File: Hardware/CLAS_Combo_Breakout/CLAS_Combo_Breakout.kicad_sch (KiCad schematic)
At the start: 77 parts, among them J1 USB_C_Receptacle_USB2.0, J2 USB_C_Receptacle_USB2.0, J3 Conn_SMA, U1 USBLC6-2P6, U2 ZED-F9P, U3 NEO-D9C-00B, U4 USBLC6-2P6, U5 LMV331, U6 AP2112K-3.3, U7 DSS20200, U8 BP2G1+, U9 NT1191GEAE3S

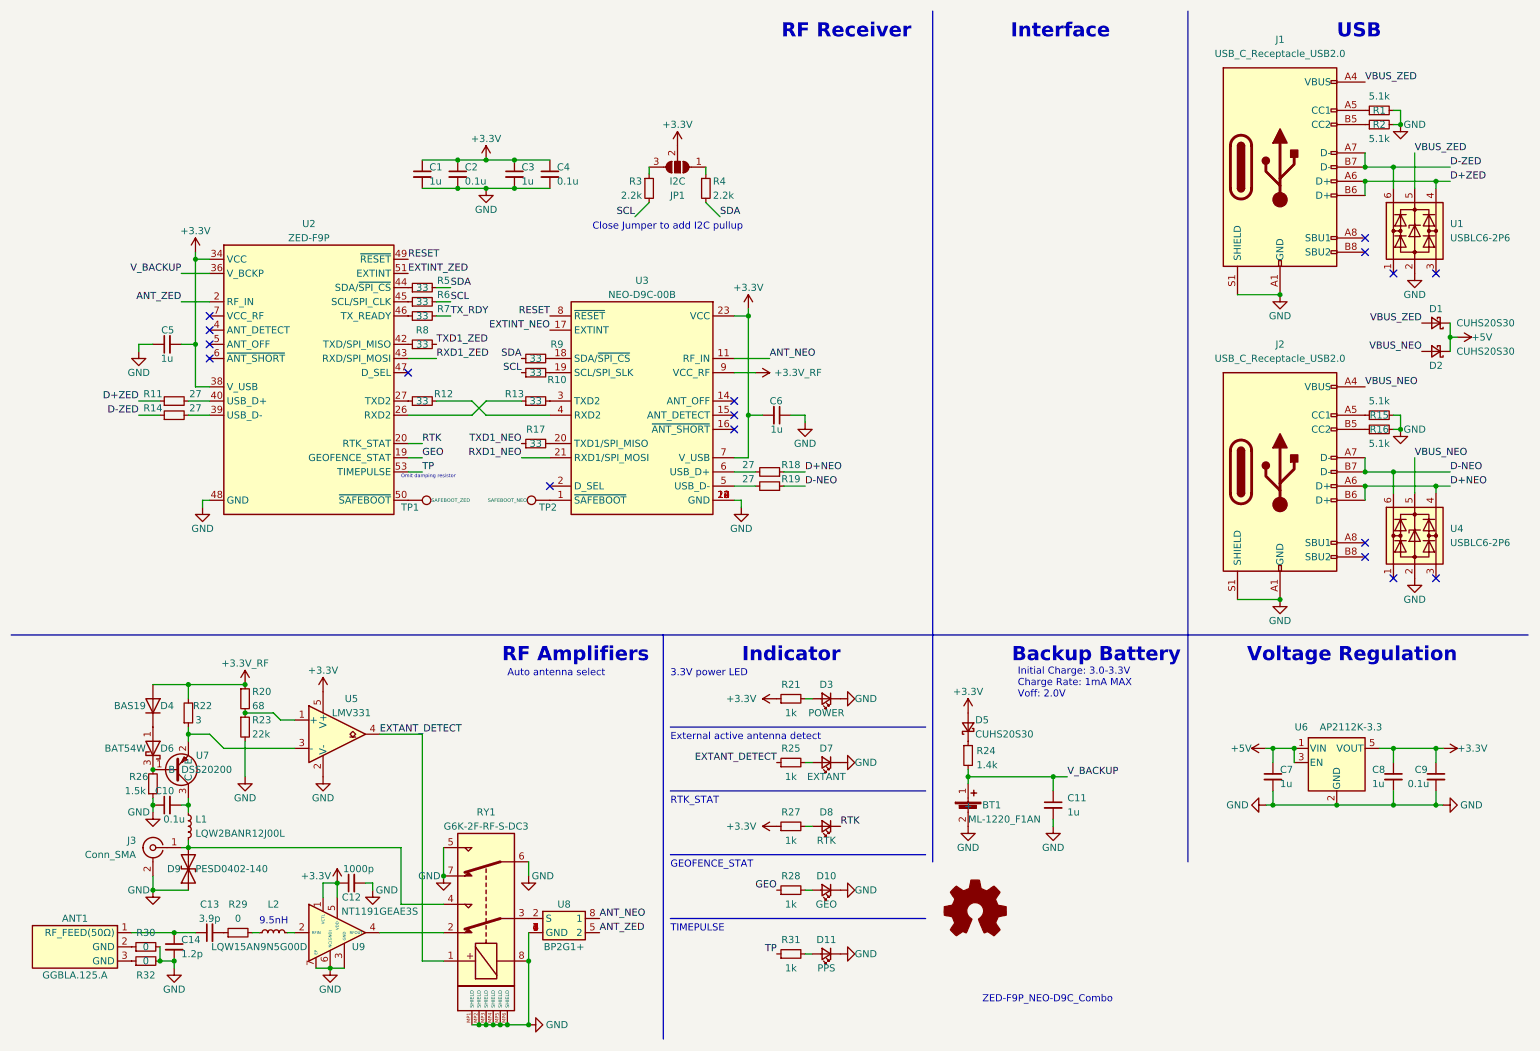
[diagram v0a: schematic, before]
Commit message: 部品を配置
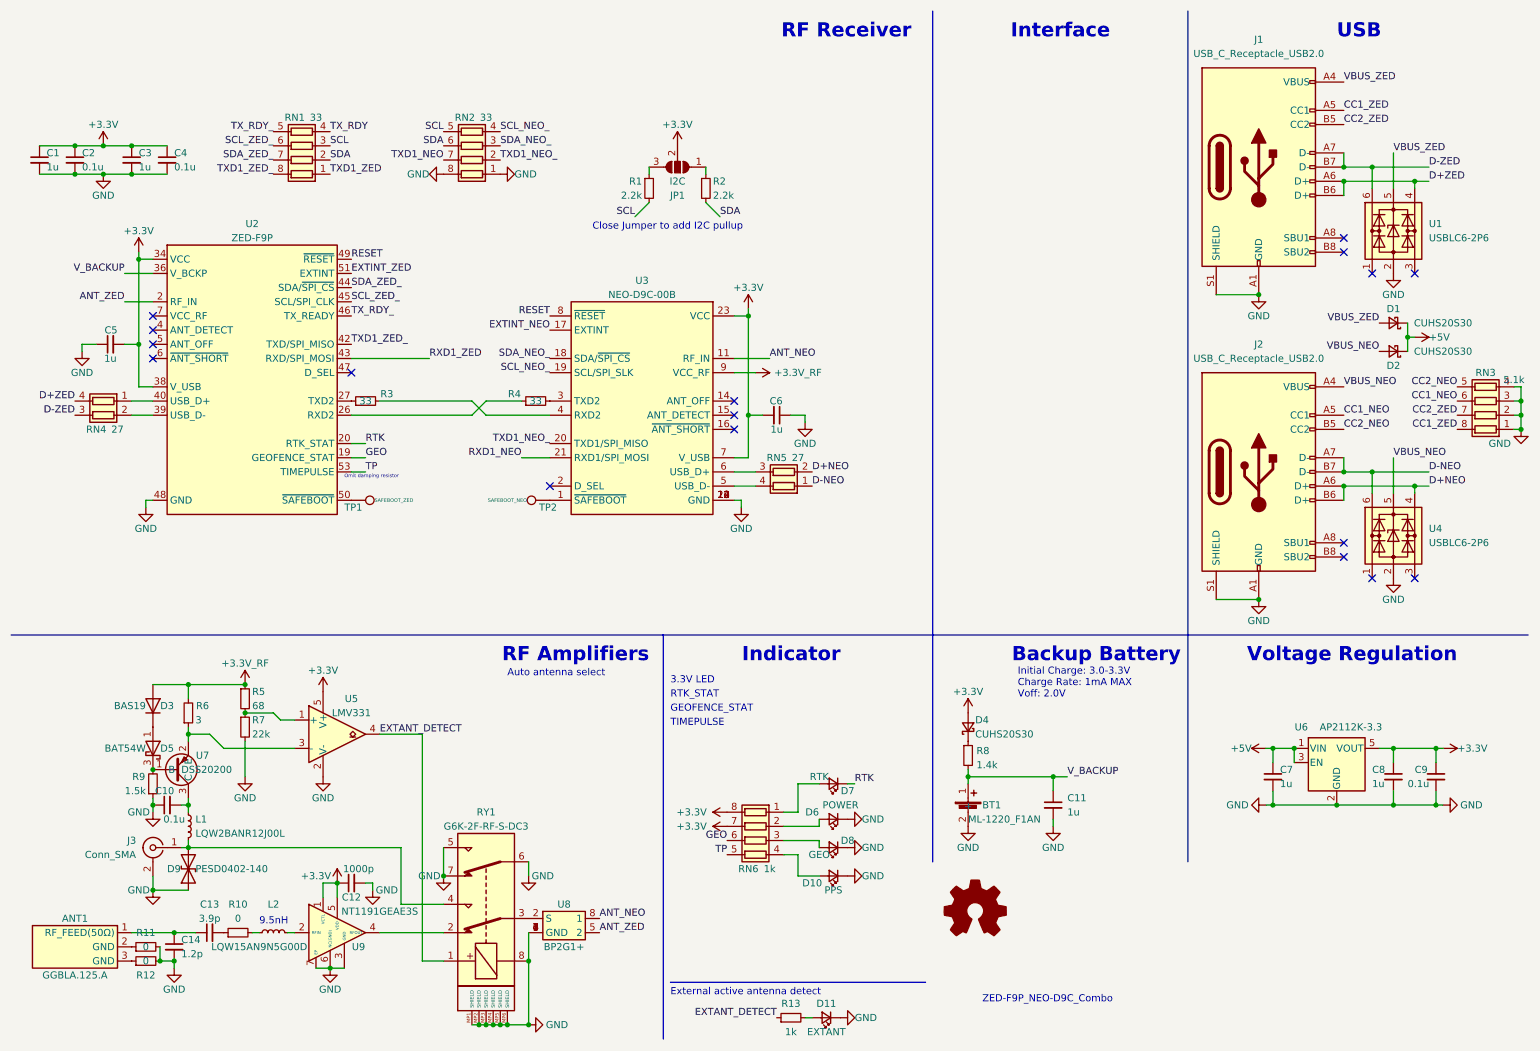
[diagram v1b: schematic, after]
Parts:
- removed R1, R15, R16, R2: 5.1k, Resistor_SMD:R_0603_1608Metric, symbol Device:R_Small
- removed R10, R17, R5, R6, R7, R8, R9: 33, Resistor_SMD:R_0603_1608Metric, symbol Device:R_Small
- removed R11, R14, R18, R19: 27, Resistor_SMD:R_0603_1608Metric, symbol Device:R_Small
- removed R21, R27, R28, R31: 1k, Resistor_SMD:R_0603_1608Metric, symbol Device:R_Small
- added RN1, RN2: 33, Resistor_SMD:R_Array_Convex_4x0402, symbol Device:R_Pack04
- added RN3: 5.1k, Resistor_SMD:R_Array_Convex_4x0402, symbol Device:R_Pack04
- added RN4, RN5: 27, Resistor_SMD:R_Array_Convex_2x0402, symbol Device:R_Pack02
- added RN6: 1k, Resistor_SMD:R_Array_Convex_4x0402, symbol Device:R_Pack04
- J1, J2: footprint Connector_USB:USB_C_Receptacle_GCT_USB4085 -> Connector_USB_extlib:USB_C_Receptacle_GCT_USB4120-03-C
- renumbered D11 to D10, D7 to D11, D4 to D3, D5 to D4, D6 to D5, D3 to D6, D8 to D7, D10 to D8, R3 to R1, R29 to R10, R30 to R11, R32 to R12, R25 to R13, R4 to R2, R12 to R3, R13 to R4, R20 to R5, R22 to R6, R23 to R7, R24 to R8, R26 to R9
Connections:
- net +3.3V: now also RN6.7 (R2.2), RN6.8 (R1.2)
- net D+NEO: now also RN5.2 (R2.1)
- net D+ZED: now also RN4.4 (R1.2)
- net D-NEO: now also RN5.1 (R1.1)
- net D-ZED: now also RN4.3 (R2.2)
- net GEO: now also RN6.6 (R3.2)
- net GND: now also RN2.1 (R1.1), RN2.8 (R1.2), RN3.1 (R1.1), RN3.2 (R2.1), RN3.3 (R3.1), RN3.4 (R4.1)
- net SCL: now also RN1.3 (R3.1), RN2.5 (R4.2)
- net SDA: now also RN1.2 (R2.1), RN2.6 (R3.2)
- net TP: now also RN6.5 (R4.2)
- net TXD1_NEO: now also RN2.7 (R2.2)
- net TXD1_ZED: now also RN1.1 (R1.1)
- net TX_RDY: now also RN1.4 (R4.1)
- net at D6.2 (A): now also RN6.2 (R2.1)
- net SCL_NEO_: now reaches U3.19 (SCL/SPI_SLK)
- net SCL_NEO_: now also RN2.4 (R4.1)
- net at D7.2 (A): now also RN6.1 (R1.1)
- net SCL_ZED_: now reaches U2.45 (SCL/SPI_CLK)
- net SCL_ZED_: now also RN1.6 (R3.2)
- net at D10.2 (A): now also RN6.4 (R4.1)
- net at U2.40 (USB_D+): now also RN4.1 (R1.1)
- net SDA_ZED_: now reaches U2.44 (SDA/~{SPI_CS})
- net SDA_ZED_: now also RN1.7 (R2.2)
- net CC1_NEO: now reaches J2.A5 (CC1)
- net CC1_NEO: now also RN3.6 (R3.2)
- net CC2_NEO: now reaches J2.B5 (CC2)
- net CC2_NEO: now also RN3.5 (R4.2)
- net TX_RDY_: now reaches U2.46 (TX_READY)
- net TX_RDY_: now also RN1.5 (R4.2)
- net CC2_ZED: now reaches J1.B5 (CC2)
- net CC2_ZED: now also RN3.7 (R2.2)
- net at D8.2 (A): now also RN6.3 (R3.1)
- net CC1_ZED: now reaches J1.A5 (CC1)
- net CC1_ZED: now also RN3.8 (R1.2)
- net at U3.6 (USB_D+): now also RN5.3 (R2.2)
- net at U2.39 (USB_D-): now also RN4.2 (R2.1)
- net TXD1_ZED_: now reaches U2.42 (TXD/SPI_MISO)
- net TXD1_ZED_: now also RN1.8 (R1.2)
- net TXD1_NEO_: now reaches U3.20 (TXD1/SPI_MISO)
- net TXD1_NEO_: now also RN2.2 (R2.1)
- net SDA_NEO_: now reaches U3.18 (SDA/~{SPI_CS})
- net SDA_NEO_: now also RN2.3 (R3.1)
- net at U3.5 (USB_D-): now also RN5.4 (R1.2)
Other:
- note added: "3.3V LED"
- note removed: "3.3V power LED"
- moved on the sheet: C1, C2, C3, C4, C5, D1, D10, D11, D2, D6, D7, D8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

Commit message: RFリレーとスプリッタを置き換え
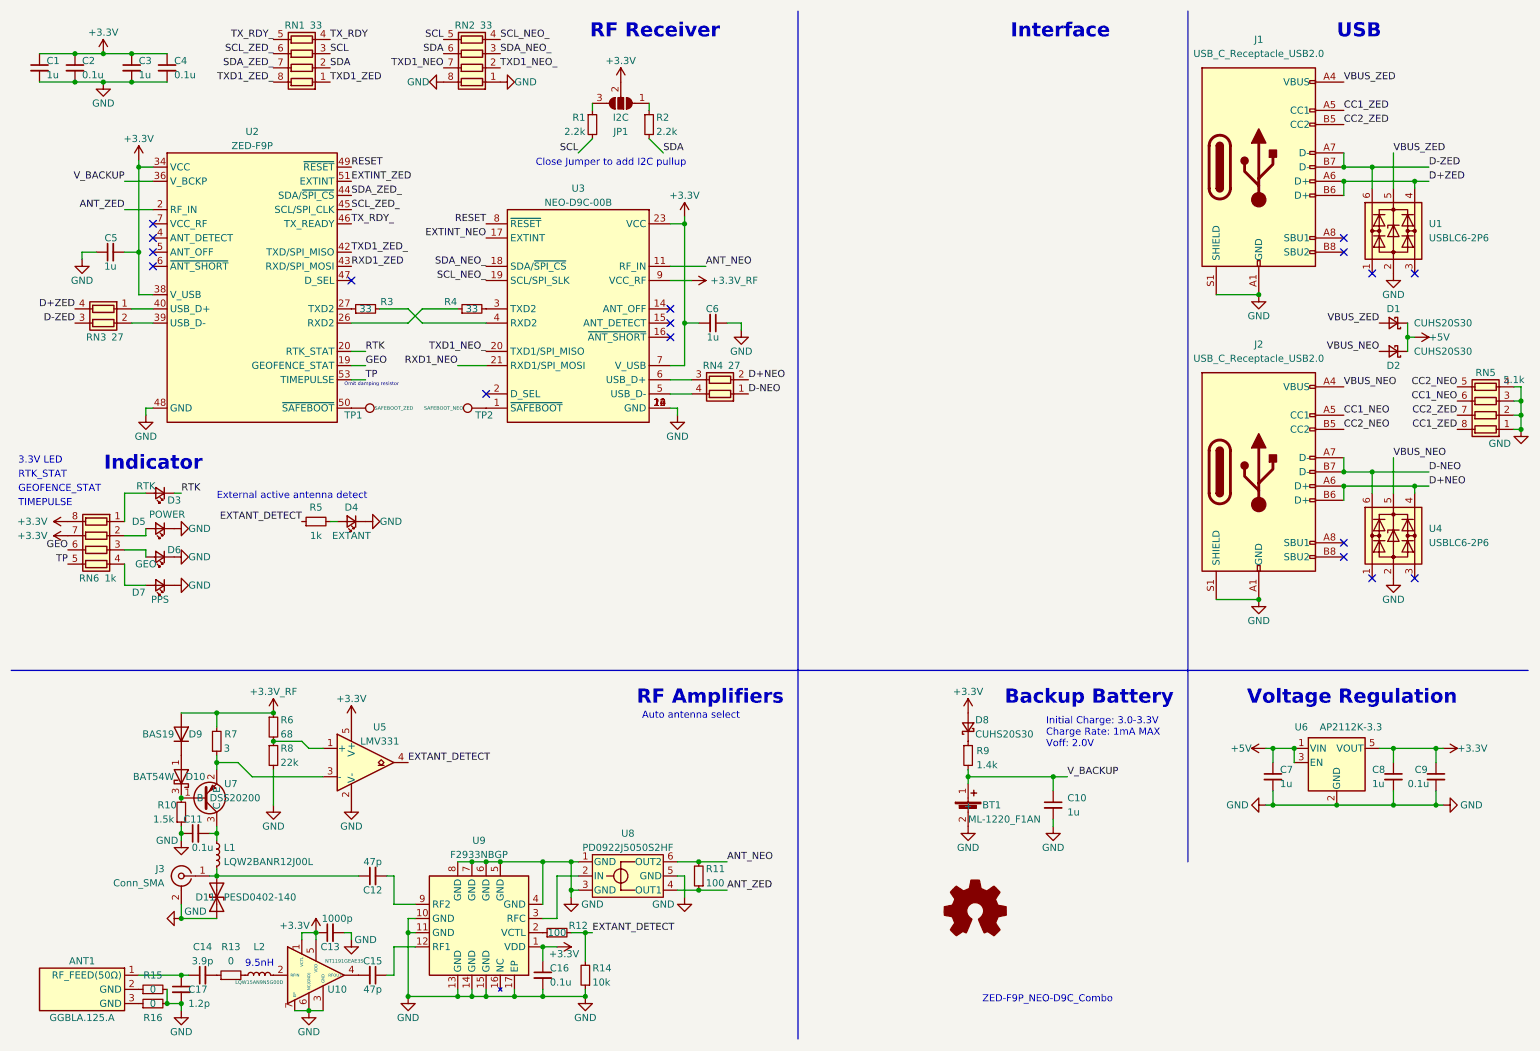
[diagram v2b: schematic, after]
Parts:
- removed RY1: G6K-2F-RF-S-DC3, G6K-2F-RF-S-DC3:G6K-2F-RF-S-DC3, symbol G6K-2F-RF-S-DC3:G6K-2F-RF-S-DC3
- removed U8: BP2G1+, BP2G1+:BP2G1, symbol BP2G1+:BP2G1+
- added C12, C15: 47p, Capacitor_SMD:C_0603_1608Metric, symbol Device:C_Small
- added C16: 0.1u, Capacitor_SMD:C_0603_1608Metric, symbol Device:C_Small
- added R11, R12: 100, Resistor_SMD:R_0603_1608Metric, symbol Device:R_Small
- added R14: 10k, Resistor_SMD:R_0603_1608Metric, symbol Device:R_Small
- added U8: PD0922J5050S2HF, PD0922J5050S2HF:PD0922J5050S2HF_ANA, symbol PD0922J5050S2HF:PD0922J5050S2HF
- added U9: F2933NBGP, F2933NBGP:F2933NBGP, symbol F2933NBGP:F2933NBGP
- renumbered C11 to C10, C10 to C11, C12 to C13, C13 to C14, C14 to C17, D5 to D10, D9 to D11, D7 to D3, D11 to D4, D6 to D5, D8 to D6, D10 to D7, D4 to D8, D3 to D9, R9 to R10, R10 to R13, R11 to R15, R12 to R16, R13 to R5, R5 to R6, R6 to R7, R7 to R8, R8 to R9, RN4 to RN3, RN5 to RN4, RN3 to RN5, U9 to U10
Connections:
- net +3.3V: now also C16.1, U9.1 (VDD)
- net ANT_NEO: now also R11.2, U8.6 (OUT2)
- net ANT_ZED: now also R11.1, U8.4 (OUT1)
- net EXTANT_DETECT: now also R12.2, R14.2
- net GND: now also C16.2, R14.1, U8.1 (GND), U8.3 (GND), U8.5 (GND), U9.10 (GND), U9.11 (GND), U9.13 (GND), U9.14 (GND), U9.15 (GND), U9.17 (EP), U9.4 (GND), U9.5 (GND), U9.6 (GND), U9.7 (GND), U9.8 (GND)
- net at U10.4 (RFOUT): now also C15.2
- net at D11.2 (A2), J3.1 (In), L1.2: now also C12.1
- new net: U8.2 (IN), U9.3 (RFC)
- new net: C15.1, U9.12 (RF1)
- new net: R12.1, U9.2 (VCTL)
- new net: C12.2, U9.9 (RF2)
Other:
- moved on the sheet: ANT1, C1, C11, C13, C14, C17, C2, C3, C4, C5, C6, D10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

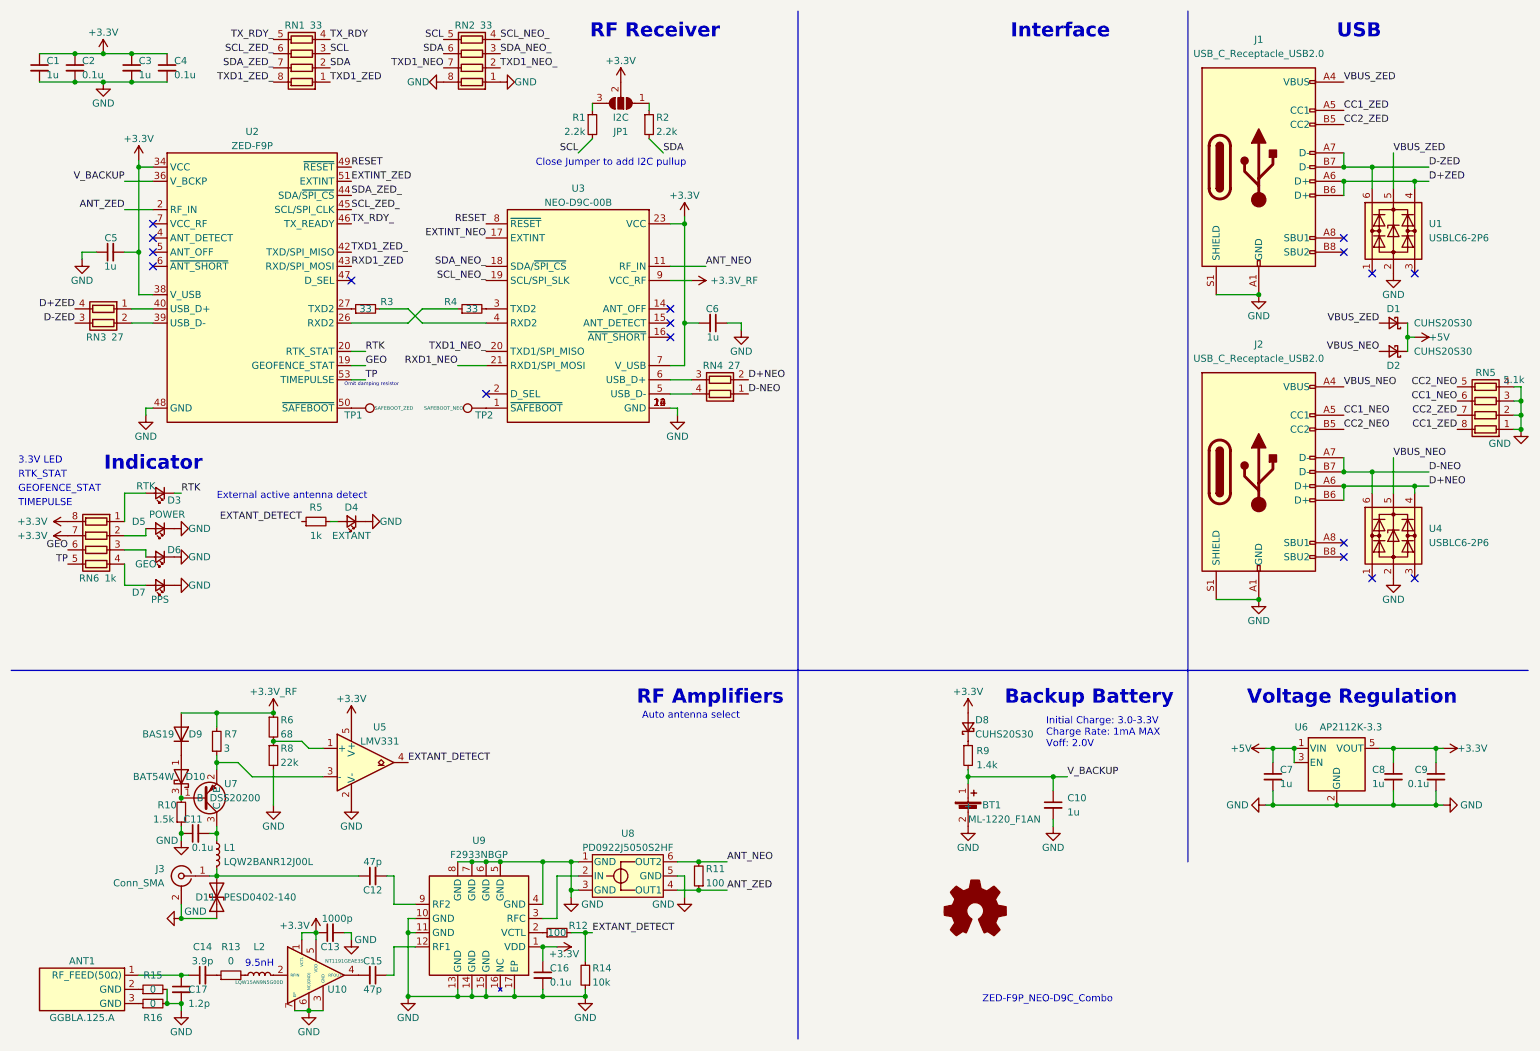
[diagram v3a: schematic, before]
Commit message: change BAT and USB_C
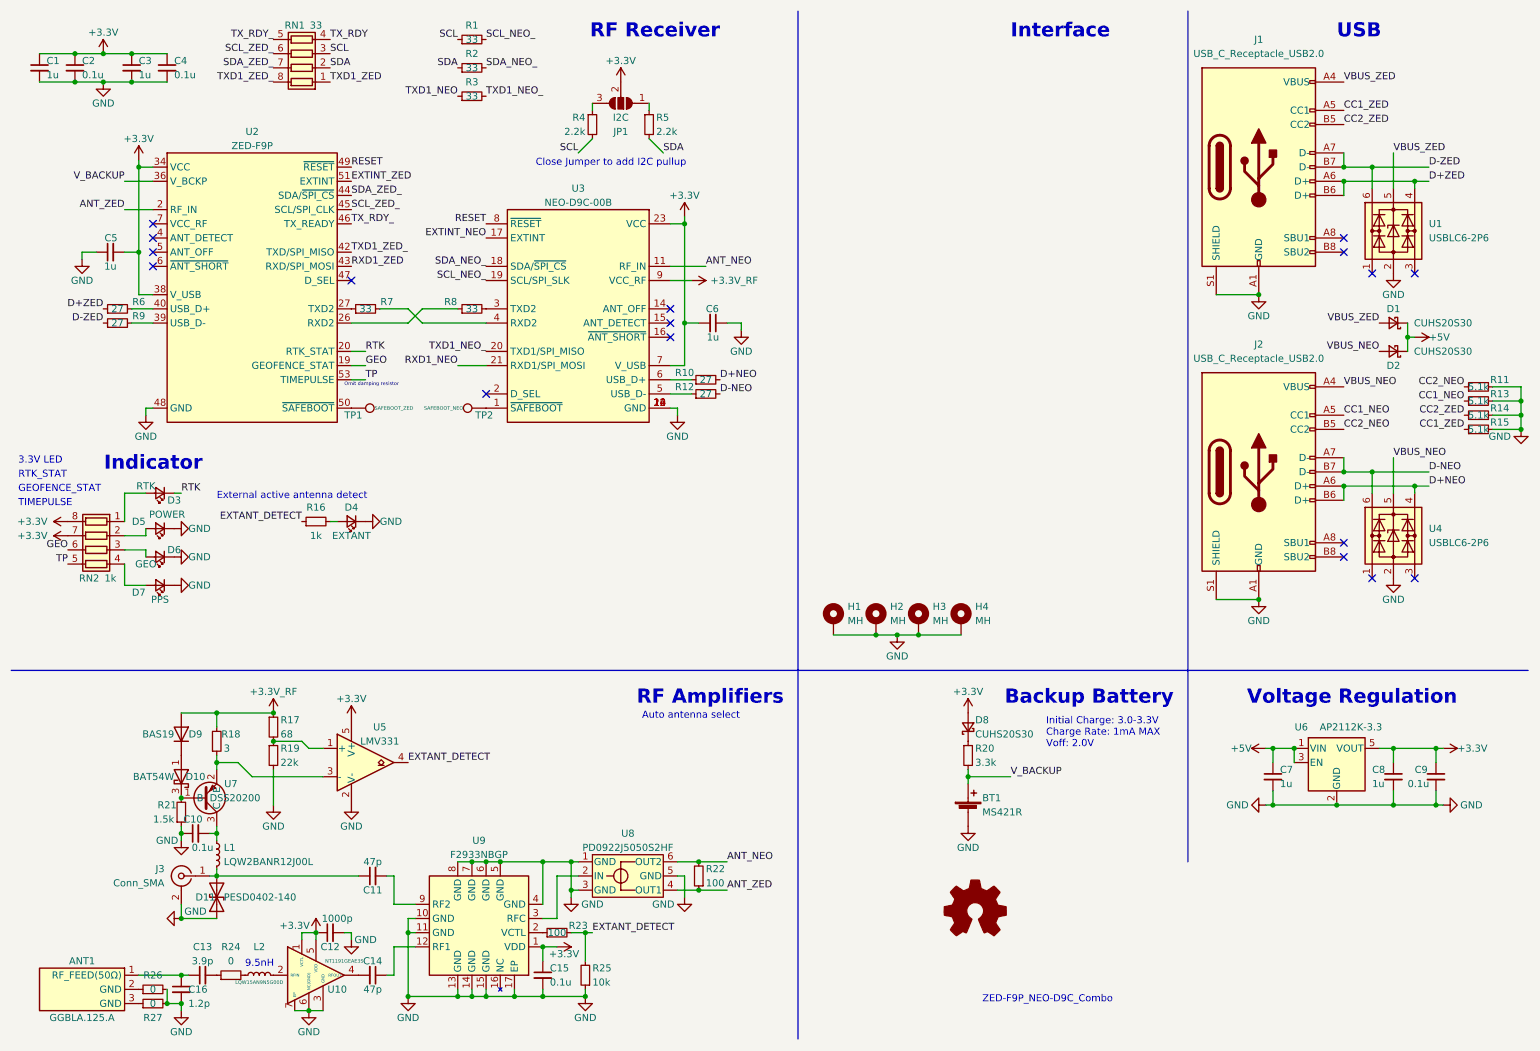
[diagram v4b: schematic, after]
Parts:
- removed BT1: ML-1220_F1AN, ML-1220_F1AN:ML-1220_F1AN, symbol ML-1220_F1AN:ML-1220_F1AN
- removed C10: 1u, Capacitor_SMD:C_0603_1608Metric, symbol Device:C_Small
- removed RN2: 33, Resistor_SMD:R_Array_Convex_4x0402, symbol Device:R_Pack04
- removed RN3, RN4: 27, Resistor_SMD:R_Array_Convex_2x0402, symbol Device:R_Pack02
- removed RN5: 5.1k, Resistor_SMD:R_Array_Convex_4x0402, symbol Device:R_Pack04
- added BT1: MS421R, Battery_extlib:MS421R, symbol Device:Battery_Cell
- added H1, H2, H3, H4: MH, MountingHole:MountingHole_2.2mm_M2_Pad_Via, symbol Mechanical:MountingHole_Pad
- added R1, R2, R3: 33, Resistor_SMD:R_0603_1608Metric, symbol Device:R_Small
- added R10, R12, R6, R9: 27, Resistor_SMD:R_0603_1608Metric, symbol Device:R_Small
- added R11, R13, R14, R15: 5.1k, Resistor_SMD:R_0603_1608Metric, symbol Device:R_Small
- J1, J2: footprint Connector_USB_extlib:USB_C_Receptacle_GCT_USB4120-03-C -> Connector_USB_extlib:USB_C_Receptacle_5077CR-16-SMC2-BK-TR
- R20: renamed from R9; value 1.4k -> 3.3k
- renumbered C11 to C10, C12 to C11, C13 to C12, C14 to C13, C15 to C14, C16 to C15, C17 to C16, R5 to R16, R6 to R17, R7 to R18, R8 to R19, R10 to R21, R11 to R22, R12 to R23, R13 to R24, R14 to R25, R15 to R26, R16 to R27, R1 to R4, R2 to R5, R3 to R7, R4 to R8, RN6 to RN2
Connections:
- net CC1_NEO: now also R13.1
- net CC1_ZED: now also R15.1
- net CC2_NEO: now also R11.1
- net CC2_ZED: now also R14.1
- net D+NEO: now also R10.2
- net D+ZED: now also R6.1
- net D-NEO: now also R12.2
- net D-ZED: now also R9.1
- net GND: now also BT1.2 (-), H1.1, H2.1, H3.1, H4.1, R11.2, R13.2, R14.2, R15.2
- net SCL: now also R1.1
- net SCL_NEO_: now also R1.2
- net SDA: now also R2.1
- net SDA_NEO_: now also R2.2
- net TXD1_NEO: now also R3.1
- net TXD1_NEO_: now also R3.2
- net V_BACKUP: now also BT1.1 (+)
- net at U2.40 (USB_D+): now also R6.2
- net at U2.39 (USB_D-): now also R9.2
- net at U3.6 (USB_D+): now also R10.1
- net at U3.5 (USB_D-): now also R12.1
